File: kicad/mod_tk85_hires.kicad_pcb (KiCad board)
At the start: 2 copper layers, 105.6 x 79 mm, 23 parts, among them IC2_PINS_13_24 PinSocket_1x12_P2.54mm_Vertic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, IC2_PINS_1_12 PinSocket_1x12_P2.54mm_Vertic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, J1 PinHeader_1x08_P2.54mm_Horizo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, U1 DIP-24_W15.24mm_Socket, U2 DIP-24_W15.24mm_Socket, U3 DIP-24_W15.24mm_Socket, U4 DIP-24_W15.24mm_Socket, U5 DIP-14_W7.62mm_Socket, U6 DIP-14_W7.62mm_Socket, U7 DIP-16_W7.62mm_Socket, U8 DIP-16_W7.62mm_Socket, U9 DIP-14_W7.62mm_Socket

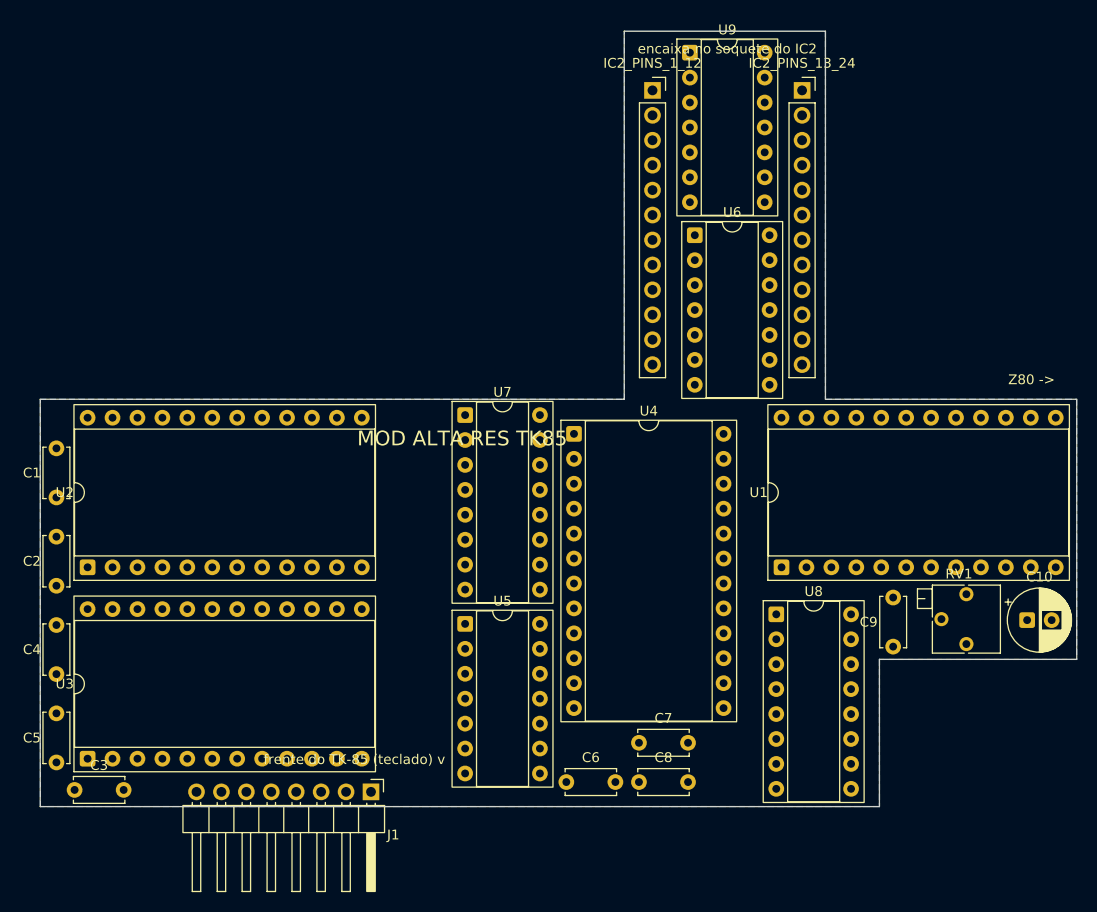
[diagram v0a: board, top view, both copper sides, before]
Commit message: PCB roteada: 2 camadas, DRC zerado
Roteamento com Freerouting 2.2.4 via pipeline DSN/SES automatizado
(placa-isca com contorno recuado 0,35 mm para garantir o isolamento
de borda; zonas removidas da isca — como plano no DSN elas bloqueiam
o autorouter; GND roteado como trilha e reforçado por pours nas duas
faces). Língua do interposer alargada 0,6 mm a oeste para abrir
corredores. Acabamento: 1 via de GND reposicionada (isolamento de
borda) e regras do projeto alinhadas ao roteado.

- Sinais 0,25 mm; +5V/GND 0,6 mm; isolamento 0,13 mm; vias 0,6/0,3
- DRC: 0 violações elétricas, 0 pads desconectados
- starved_thermal rebaixado a aviso (4 pads de GND com 1 raio de
  zona, todos com conexão plena por trilha) — docs/mecanica.md
- Exportado esquemas/mod_tk85_hires_pcb.pdf

Co-Authored-By: Claude Fable 5 <noreply@anthropic.com>
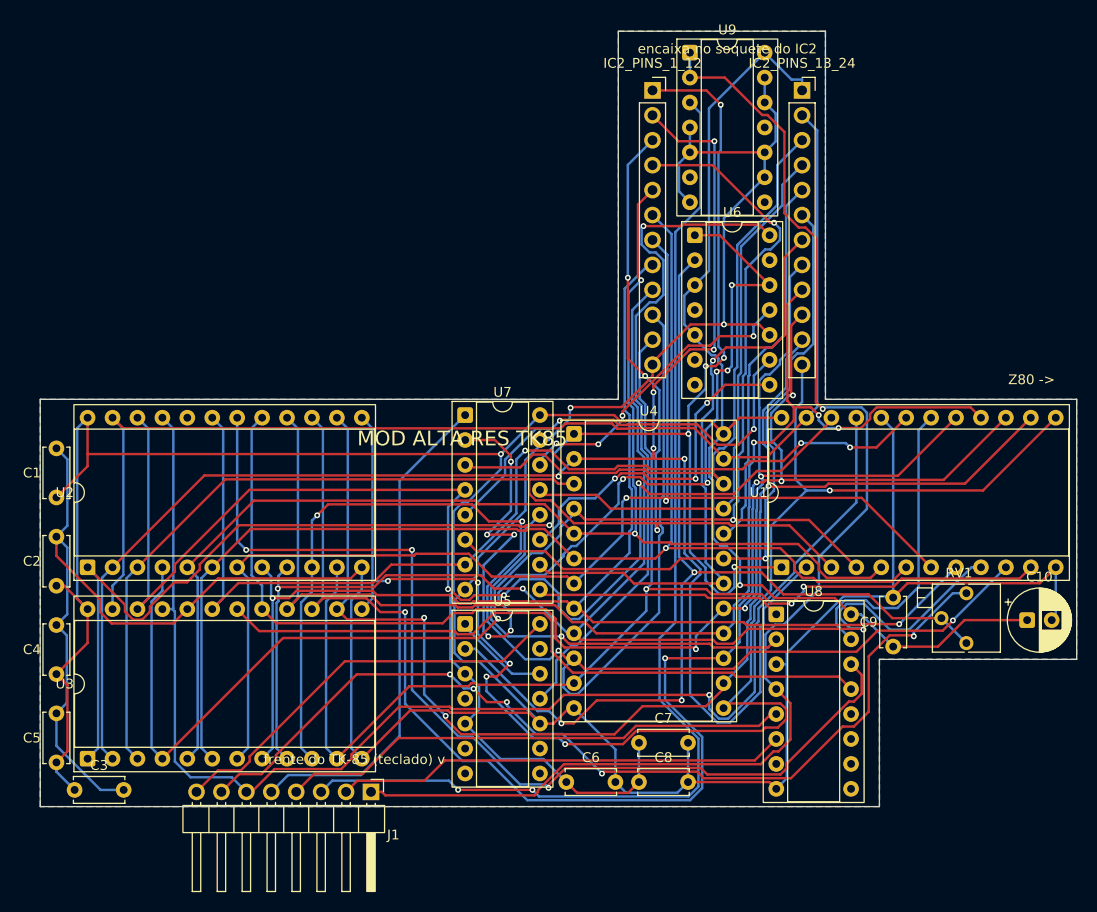
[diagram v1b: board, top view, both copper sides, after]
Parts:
- moved RV1 0.10 mm to (174.4, 137.3)
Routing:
- net GND: track 0.00 -> 339.0 mm, vias 0 -> 2
- net +5V: track 0.00 -> 286.9 mm, vias 0 -> 2
- net /A6: track 0.00 -> 176.8 mm, vias 0 -> 6
- net /D1: track 0.00 -> 167.6 mm, vias 0 -> 4
- net /A7: track 0.00 -> 166.7 mm, vias 0 -> 6
- net /D5: track 0.00 -> 162.5 mm, vias 0 -> 5
- net /D3: track 0.00 -> 155.0 mm, vias 0 -> 6
- net /A4: track 0.00 -> 154.8 mm, vias 0 -> 3
- net /A5: track 0.00 -> 147.2 mm, vias 0 -> 3
- net /D0: track 0.00 -> 145.6 mm, vias 0 -> 3
- net /D4: track 0.00 -> 140.9 mm, vias 0 -> 3
- net /WR: track 0.00 -> 136.8 mm, vias 0 -> 1
- net /D7: track 0.00 -> 136.5 mm, vias 0 -> 3
- net /A3: track 0.00 -> 134.5 mm, vias 0 -> 2
- net /A14: track 0.00 -> 134.0 mm, vias 0 -> 1
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- added copper zone on F.Cu, net GND
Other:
- outline, holes or cut-outs redrawn

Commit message: Silk: limpeza manual (topo) e pinagem do J1 no verso
- Limpeza dos textos de silkscreen no topo feita manualmente no
  pcbnew (62 -> 9 avisos, nenhum silk sobre cobre)
- Novo rótulo espelhado no B.SilkS com a pinagem do J1 (1=A14,
  2=A15, 3=RAM_CS, 4=MREQ, 5=RFSH, 6=WR, 7=CLK_60, 8=CLK_VID),
  posicionado entre as fileiras de pads do U3, sem criar nenhum
  aviso novo de DRC
- .history/ do editor adicionado ao .gitignore

Co-Authored-By: Claude Fable 5 <noreply@anthropic.com>
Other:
- board text added: "J1 (pino 1 = lado do Z80) 1 A14 5 RFSH 2 A15 6 WR 3 RAM_CS 7 CLK_60 4 MREQ 8 CLK_VID"
- board text added: "MOD ALTA RES TK85 MMJ"
- board text added: "Z80>"
- board text added: "frente do TK-85"
- board text removed: "MOD ALTA RES TK85"
- board text removed: "Z80 ->"
- board text removed: "frente do TK-85 (teclado) v"
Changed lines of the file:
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@@
 		(tags "C Disc series Radial pin pitch 5.00mm diameter 5mm width 2.5mm Capacitor")
 		(property "Reference" "C4"
-			(at 2.5 -2.5 0)
+			(at 6.7 -0.15 0)
 			(layer "F.SilkS")
 			(effects
@@
 		(tags "C Disc series Radial pin pitch 5.00mm diameter 5mm width 2.5mm Capacitor")
 		(property "Reference" "C7"
-			(at 2.5 -2.5 0)
+			(at 7.5 0 0)
 			(layer "F.SilkS")
 			(effects
@@
 		(tags "Through hole angled pin header THT 1x08 2.54mm single row")
 		(property "Reference" "J1"
-			(at 4.385 -2.27 0)
+			(at 0 -2.8 0)
 			(layer "F.SilkS")
 			(effects
@@
 		(tags "THT DIP DIL PDIP 2.54mm 15.24mm 600mil Socket")
 		(property "Reference" "U2"
-			(at 7.62 -2.33 0)
+			(at 8.62 30.675 0)
 			(layer "F.SilkS")
 			(effects
@@
 		(tags "THT DIP DIL PDIP 2.54mm 7.62mm 300mil Socket")
 		(property "Reference" "U5"
-			(at 3.81 -2.33 0)
+			(at 3.71 6.615 0)
 			(layer "F.SilkS")
 			(effects
@@
 		(tags "THT DIP DIL PDIP 2.54mm 15.24mm 600mil Socket")
 		(property "Reference" "U1"
-			(at 7.62 -2.33 0)
+			(at 7.62 -2.525 0)
 			(layer "F.SilkS")
 			(effects
@@
 		(tags "C Disc series Radial pin pitch 5.00mm diameter 5mm width 2.5mm Capacitor")
 		(property "Reference" "C3"
-			(at 2.5 -2.5 0)
+			(at 7 0.2 0)
 			(layer "F.SilkS")
 			(effects
@@
 		(tags "THT DIP DIL PDIP 2.54mm 7.62mm 300mil Socket")
 		(property "Reference" "U9"
-			(at 3.81 -2.33 0)
+			(at 3.81 7.815 0)
 			(layer "F.SilkS")
 			(effects
@@
 		(tags "C Disc series Radial pin pitch 5.00mm diameter 5mm width 2.5mm Capacitor")
 		(property "Reference" "C9"
-			(at 2.5 -2.5 0)
+			(at 5.7 -2.5 0)
 			(layer "F.SilkS")
 			(effects
@@
 		(tags "CP Radial series Radial pin pitch 2.50mm diameter 6.3mm height 7mm Electrolytic Capacitor")
 		(property "Reference" "C10"
-			(at 1.25 -4.4 0)
+			(at -0.75 2.4 0)
 			(layer "F.SilkS")
 			(effects
@@
 		(tags "THT DIP DIL PDIP 2.54mm 7.62mm 300mil Socket")
 		(property "Reference" "U8"
-			(at 3.81 -2.33 0)
+			(at 4.01 -2.33 0)
 			(layer "F.SilkS")
 			(effects
@@
 		(tags "Potentiometer horizontal Bourns 3266P")
 		(property "Reference" "RV1"
-			(at -0.76 -2.065 0)
+			(at 0.64 2.74 0)
 			(layer "F.SilkS")
 			(effects
@@
 		(tags "C Disc series Radial pin pitch 5.00mm diameter 5mm width 2.5mm Capacitor")
 		(property "Reference" "C8"
-			(at 2.5 -2.5 0)
+			(at 7.5 0 0)
 			(layer "F.SilkS")
 			(effects
@@
 		(tags "THT DIP DIL PDIP 2.54mm 15.24mm 600mil Socket")
 		(property "Reference" "U3"
-			(at 7.62 -2.33 0)
+			(at 8.62 30.675 0)
 			(layer "F.SilkS")
 			(effects
@@
 			(at 0 -2.77 0)
 			(layer "F.SilkS")
+			(hide yes)
 			(effects
 				(font
@@
 		(tags "C Disc series Radial pin pitch 5.00mm diameter 5mm width 2.5mm Capacitor")
 		(property "Reference" "C2"
-			(at 2.5 -2.5 0)
+			(at 6.7 -0.15 0)
 			(layer "F.SilkS")
 			(effects
@@
 		(tags "THT DIP DIL PDIP 2.54mm 7.62mm 300mil Socket")
 		(property "Reference" "U6"
-			(at 3.81 -2.33 0)
+			(at 3.81 7.715 0)
 			(layer "F.SilkS")
 			(effects
@@
 			(at 0 -2.77 0)
 			(layer "F.SilkS")
+			(hide yes)
 			(effects
 				(font
@@
 		(tags "C Disc series Radial pin pitch 5.00mm diameter 5mm width 2.5mm Capacitor")
 		(property "Reference" "C5"
-			(at 2.5 -2.5 0)
+			(at 6.7 -0.15 0)
 			(layer "F.SilkS")
 			(effects
@@
 		)
 		(property "Value" "C_Disc_D5.0mm_W2.5mm_P5.00mm"
-			(at 2.5 2.5 0)
+			(at 1 -4.65 0)
 			(layer "F.Fab")
 			(effects
@@
 		(tags "THT DIP DIL PDIP 2.54mm 7.62mm 300mil Socket")
 		(property "Reference" "U7"
-			(at 3.81 -2.33 0)
+			(at 4.21 7.89 0)
 			(layer "F.SilkS")
 			(effects
@@
 		(tags "C Disc series Radial pin pitch 5.00mm diameter 5mm width 2.5mm Capacitor")
 		(property "Reference" "C1"
-			(at 2.5 -2.5 0)
+			(at 6.7 -0.15 0)
 			(layer "F.SilkS")
 			(effects
@@
 		(layer "Edge.Cuts")
 	)
-	(gr_text "frente do TK-85 (teclado) v"
-		(at 112 154.2 0)
+	(gr_text "frente do TK-85"
+		(at 125.8 158.1 0)
 		(layer "F.SilkS")
 		(effects
@@
 		)
 	)
-	(gr_text "encaixa no soquete do IC2"
-		(at 150 81.8 0)
+	(gr_text "Z80>"
+		(at 157.6 81.5 0)
 		(layer "F.SilkS")
 		(effects
@@
 		)
 	)
-	(gr_text "Z80 ->"
-		(at 181 115.5 0)
+	(gr_text "encaixa no soquete do IC2"
+		(at 139.9 100.5 90)
 		(layer "F.SilkS")
 		(effects
@@
 		)
 	)
-	(gr_text "MOD ALTA RES TK85"
-		(at 123 121.5 0)
+	(gr_text "MOD ALTA RES TK85 MMJ"
+		(at 118.5 138.5 90)
 		(layer "F.SilkS")
 		(effects
@@
 		)
 	)
+	(gr_text "J1 (pino 1 = lado do Z80)\n1 A14     5 RFSH\n2 A15     6 WR\n3 RAM_CS  7 CLK_60\n4 MREQ    8 CLK_VID"
+		(at 108.5 141.3 0)
+		(layer "B.SilkS")
+		(effects
+			(font
+				(size 1 1)
+				(thickness 0.15)
+			)
+			(justify left top mirror)
+		)
+	)

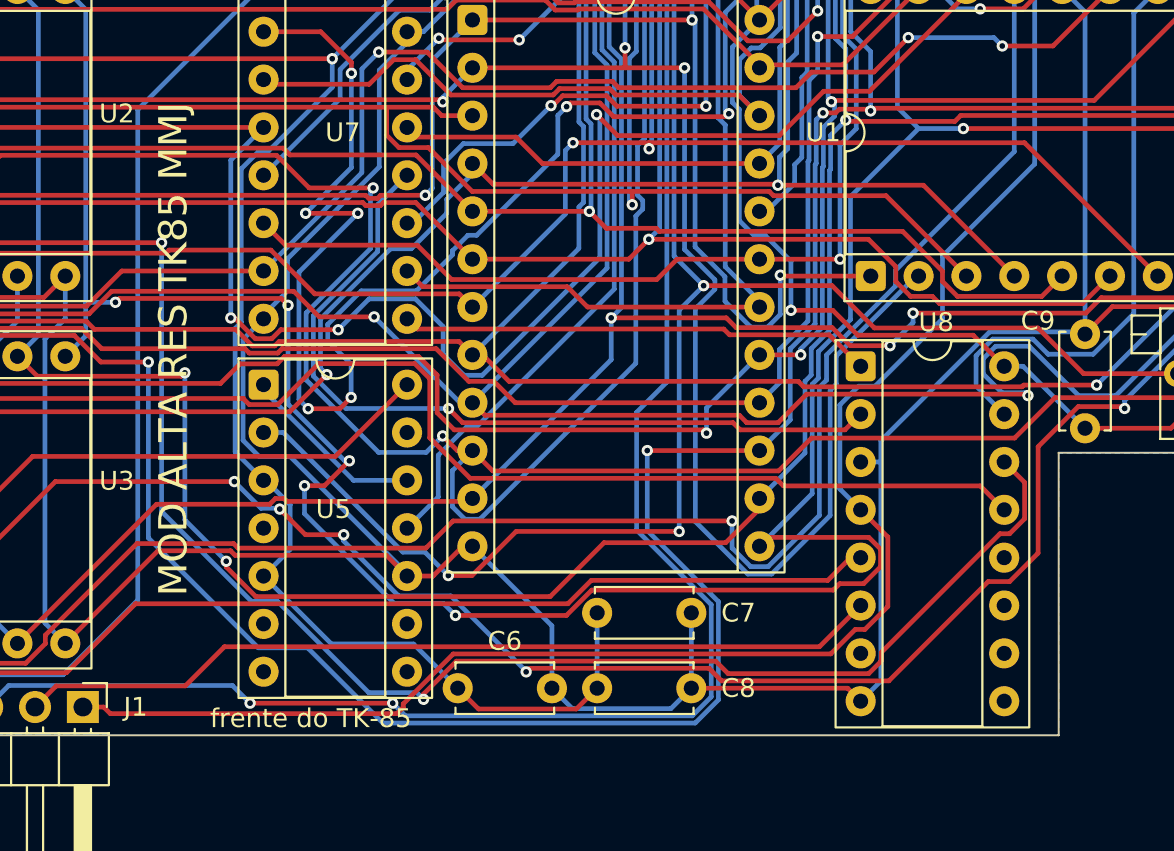
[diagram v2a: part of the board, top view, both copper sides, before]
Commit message: Referência do artigo (Datassette) e arquivos de fabricação
- referencias.md: link do acervo Datassette para consulta do artigo
  original da Microhobby
- fabricacao/: Gerbers X2 (7 camadas), furação Excellon com mapa,
  zip pronto para fábrica e README com a especificação da placa
  (2 camadas, 1,6 mm, trilha mín. 0,25 mm, isolamento 0,13 mm,
  furo mín. 0,3 mm — dentro do padrão barato de qualquer fabricante)

Co-Authored-By: Claude Fable 5 <noreply@anthropic.com>
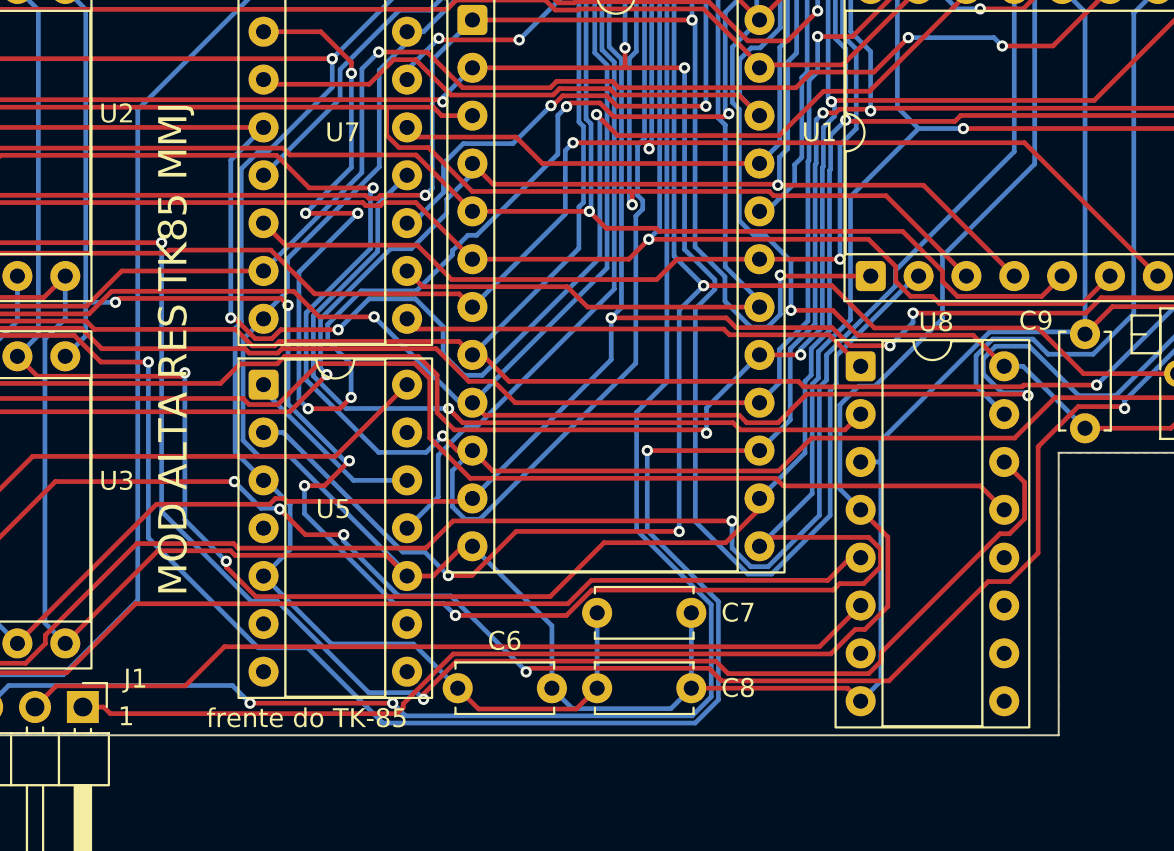
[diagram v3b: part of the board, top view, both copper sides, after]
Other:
- board text added: "1"
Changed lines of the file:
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@@
 		(tags "Through hole angled pin header THT 1x08 2.54mm single row")
 		(property "Reference" "J1"
-			(at 0 -2.8 0)
+			(at -1.5 -2.8 0)
 			(layer "F.SilkS")
 			(effects
@@
 		(tags "THT DIP DIL PDIP 2.54mm 15.24mm 600mil Socket")
 		(property "Reference" "U1"
-			(at 7.62 -2.525 0)
+			(at 7.62 -2.725 0)
 			(layer "F.SilkS")
 			(effects
@@
 		(tags "C Disc series Radial pin pitch 5.00mm diameter 5mm width 2.5mm Capacitor")
 		(property "Reference" "C9"
-			(at 5.7 -2.5 0)
+			(at 5.7 -2.6 0)
 			(layer "F.SilkS")
 			(effects
@@
 		(layer "Edge.Cuts")
 	)
+	(gr_text "1"
+		(at 116 158 0)
+		(layer "F.SilkS")
+		(effects
+			(font
+				(size 1 1)
+				(thickness 0.15)
+			)
+		)
+	)
 	(gr_text "frente do TK-85"
-		(at 125.8 158.1 0)
+		(at 125.6 158.1 0)
 		(layer "F.SilkS")
 		(effects
@@
 	)
 	(gr_text "J1 (pino 1 = lado do Z80)\n1 A14     5 RFSH\n2 A15     6 WR\n3 RAM_CS  7 CLK_60\n4 MREQ    8 CLK_VID"
-		(at 108.5 141.3 0)
+		(at 113.5 143 0)
 		(layer "B.SilkS")
 		(effects

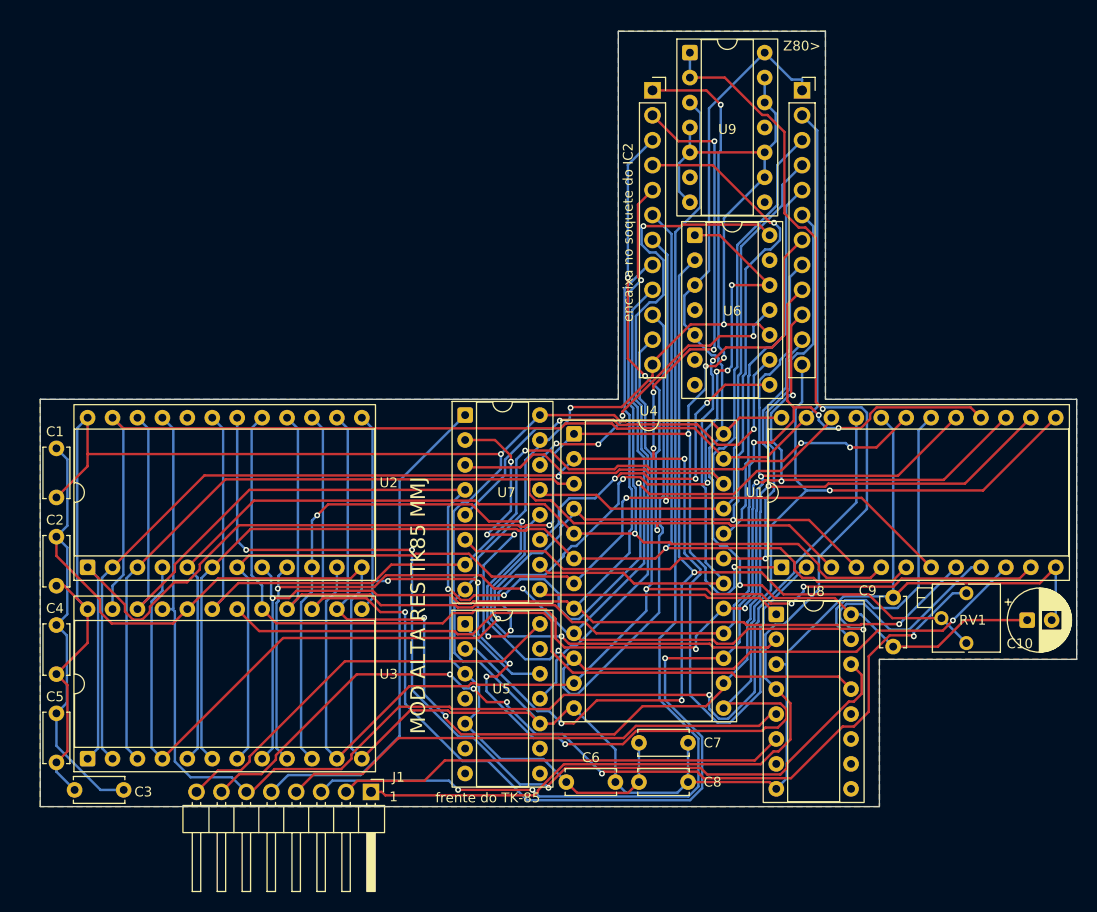
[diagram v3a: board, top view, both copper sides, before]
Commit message: RV1 com ajuste por cima (3266W), silk do usuário e opção ROM-na-língua
- RV1 trocado de Bourns 3266P (lateral — parafuso ficava voltado
  para o interior da placa, inacessível) para 3266W (ajuste pelo
  topo), mantendo os pads 1/2 nas posições originais; /CS0 foi
  re-roteado para liberar o novo pad 3, e o courtyard embutido do
  footprint foi aparado 0,25 mm (corpos reais ficam ~1 mm afastados
  de U1/C9). DRC: 0 violações elétricas, 0 pads desconectados
- Ajustes manuais de silkscreen do usuário incluídos
- docs/mecanica.md: montagem da ROM diretamente sobre a língua do
  interposer (as nets dos pentes são idênticas às de U4, pino a
  pino) usando soquete DIP-24 torneado wire-wrap; U4 fica
  despopulado nessa opção. Nota sobre o RV1
- BOM atualizada (footprints _Socket/W7.62 corretos e 3266W);
  esquema com o campo de footprint do RV1 atualizado
- Gerbers, furação, zip e PDF da placa regenerados

Co-Authored-By: Claude Fable 5 <noreply@anthropic.com>
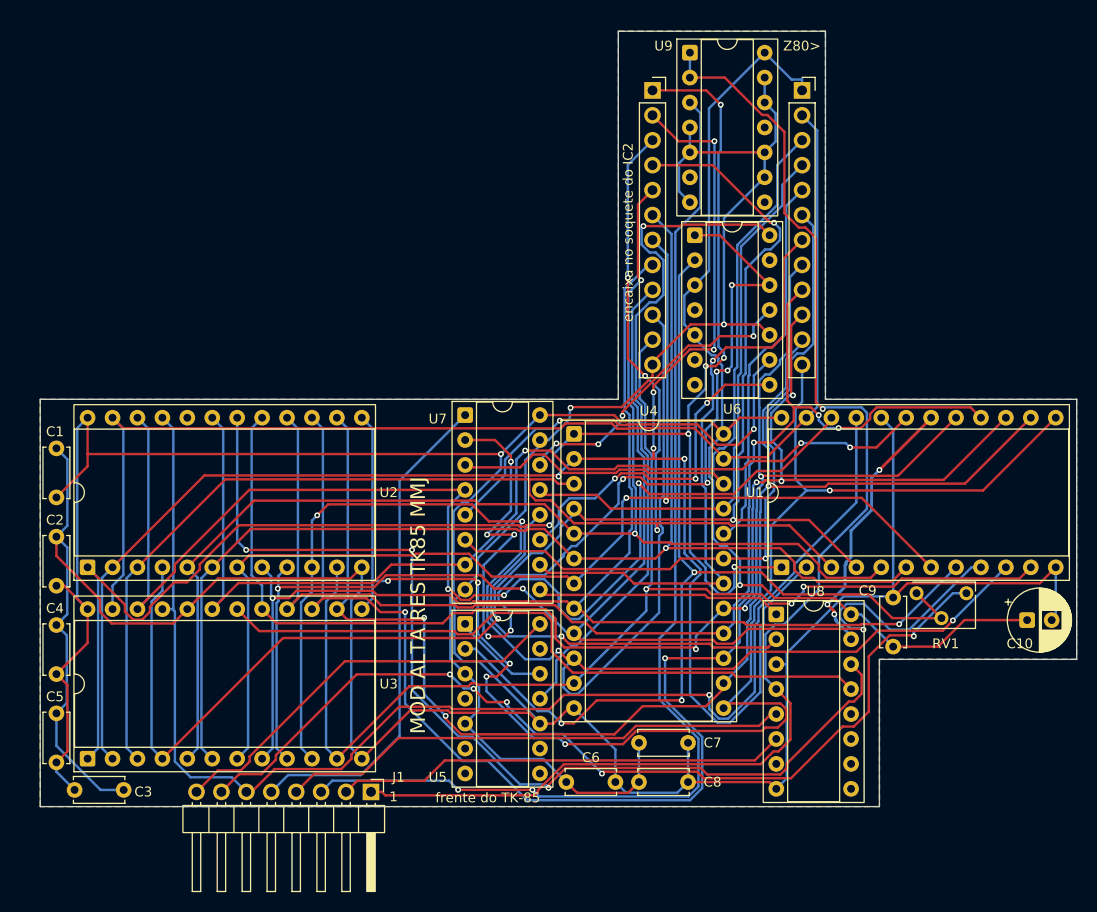
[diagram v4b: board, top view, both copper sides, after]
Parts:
- RV1: value Potentiometer_Bourns_3266P_Horizontal -> 22K; footprint Potentiometer_THT:Potentiometer_Bourns_3266P_Horizontal -> Potentiometer_Bourns_3266W_Vertical
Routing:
- net /CS0: track 31.4 -> 27.9 mm, vias 0 -> 3
